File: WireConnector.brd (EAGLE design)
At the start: 15.2 x 20.3 mm, 2 parts

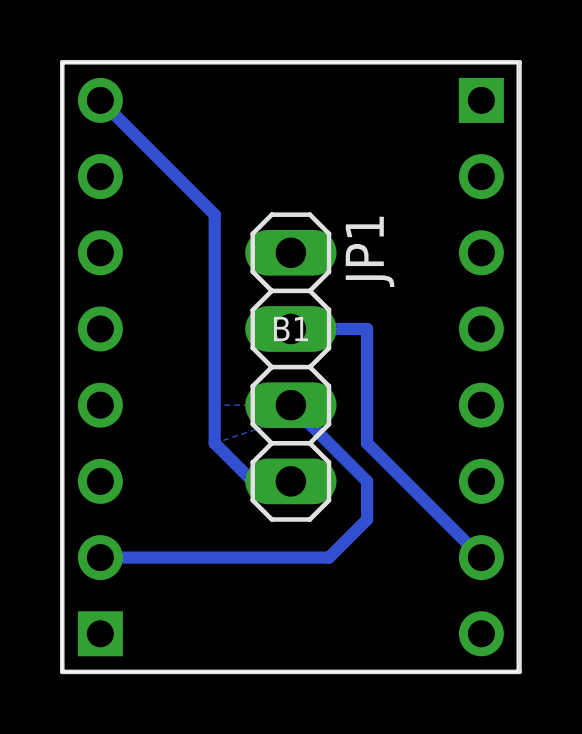
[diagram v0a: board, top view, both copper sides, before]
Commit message: Changed PWR connection position 2 Layer design GND Plate both sites Naming completed
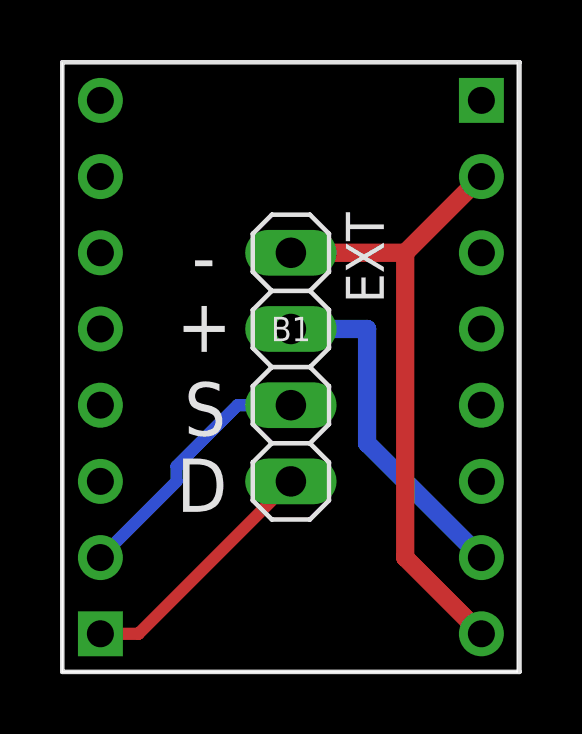
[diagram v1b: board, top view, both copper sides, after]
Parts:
- renumbered JP1 to EXT
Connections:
- net N$4: now also B1.DIR; no longer B1.EN
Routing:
- net GND: track 0.00 -> 21.2 mm
- net N$4: track 16.1 -> 8.45 mm
- net N$3: track 14.3 -> 8.75 mm
- added copper zone on layer 1, net GND
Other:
- board text added: "+"
- board text added: "-"
- board text added: "D"
- board text added: "S"
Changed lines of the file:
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@@
 <?xml version="1.0" encoding="utf-8"?>
 <!DOCTYPE eagle SYSTEM "eagle.dtd">
-<eagle version="7.2.0">
+<eagle version="7.7.0">
 <drawing>
 <settings>
@@
 <wire x1="26.67" y1="40.64" x2="41.834" y2="40.64" width="0" layer="20"/>
 <wire x1="41.834" y1="40.64" x2="41.834" y2="60.95" width="0" layer="20"/>
-<wire x1="41.834" y1="60.95" x2="26.67" y2="60.95" width="0" layer="20"/>
 <wire x1="26.67" y1="60.95" x2="26.67" y2="40.64" width="0" layer="20"/>
+<text x="30.988" y="53.594" size="1.778" layer="25">-</text>
+<text x="30.48" y="51.308" size="1.778" layer="25">+</text>
+<text x="30.734" y="48.514" size="1.778" layer="25">S</text>
+<text x="30.48" y="45.974" size="1.778" layer="25">D</text>
 </plain>
 <attributes>
@@
 </class>
 </classes>
-<designrules name="default">
+<designrules name="default *">
 <description language="de">&lt;b&gt;EAGLE Design Rules&lt;/b&gt;
 &lt;p&gt;
@@
 <param name="mdViaViaSameLayer" value="8mil"/>
 <param name="mnLayersViaInSmd" value="2"/>
-<param name="mdCopperDimension" value="40mil"/>
+<param name="mdCopperDimension" value="10mil"/>
 <param name="mdDrill" value="8mil"/>
 <param name="mdSmdStop" value="0mil"/>
@@
 <autorouter>
 <pass name="Default">
-<param name="RoutingGrid" value="50mil"/>
+<param name="RoutingGrid" value="12.5mil"/>
 <param name="AutoGrid" value="1"/>
 <param name="Efforts" value="0"/>
 <param name="TopRouterVariant" value="1"/>
 <param name="tpViaShape" value="round"/>
-<param name="PrefDir.1" value="a"/>
+<param name="PrefDir.1" value="-"/>
 <param name="PrefDir.2" value="0"/>
 <param name="PrefDir.3" value="0"/>
@@
 <param name="PrefDir.14" value="0"/>
 <param name="PrefDir.15" value="0"/>
-<param name="PrefDir.16" value="a"/>
+<param name="PrefDir.16" value="|"/>
 <param name="cfVia" value="8"/>
 <param name="cfNonPref" value="5"/>
@@
 <elements>
 <element name="B1" library="we-board" package="STEPSTICK_TP" value="STEPSTICK-TP" x="34.29" y="50.8"/>
-<element name="JP1" library="pinhead" package="1X04" value="" x="34.29" y="50.8" rot="R270"/>
+<element name="EXT" library="pinhead" package="1X04" value="" x="34.29" y="50.8" rot="R270"/>
 </elements>
 <signals>
@@
 </signal>
 <signal name="N$2" class="2">
-<contactref element="JP1" pad="2"/>
+<contactref element="EXT" pad="2"/>
 <contactref element="B1" pad="VIO"/>
-<wire x1="34.29" y1="52.07" x2="36.83" y2="52.07" width="0.4064" layer="16"/>
-<wire x1="36.83" y1="52.07" x2="36.83" y2="48.26" width="0.4064" layer="16"/>
-<wire x1="36.83" y1="48.26" x2="40.64" y2="44.45" width="0.4064" layer="16"/>
+<wire x1="34.29" y1="52.07" x2="36.83" y2="52.07" width="0.6096" layer="16"/>
+<wire x1="36.83" y1="52.07" x2="36.83" y2="48.26" width="0.6096" layer="16"/>
+<wire x1="36.83" y1="48.26" x2="40.64" y2="44.45" width="0.6096" layer="16"/>
 </signal>
 <signal name="N$3" class="1">
-<contactref element="JP1" pad="3"/>
+<contactref element="EXT" pad="3"/>
 <contactref element="B1" pad="STEP"/>
-<wire x1="34.29" y1="49.53" x2="36.83" y2="46.99" width="0.4064" layer="16"/>
-<wire x1="36.83" y1="46.99" x2="36.83" y2="45.72" width="0.4064" layer="16"/>
-<wire x1="36.83" y1="45.72" x2="35.56" y2="44.45" width="0.4064" layer="16"/>
-<wire x1="35.56" y1="44.45" x2="27.94" y2="44.45" width="0.4064" layer="16"/>
+<wire x1="27.94" y1="44.45" x2="30.48" y2="46.99" width="0.4064" layer="16"/>
+<wire x1="30.48" y1="46.99" x2="30.48" y2="47.498" width="0.4064" layer="16"/>
+<wire x1="30.48" y1="47.498" x2="32.512" y2="49.53" width="0.4064" layer="16"/>
+<wire x1="32.512" y1="49.53" x2="34.29" y2="49.53" width="0.4064" layer="16"/>
 </signal>
 <signal name="N$4" class="2">
-<contactref element="JP1" pad="4"/>
-<contactref element="B1" pad="EN"/>
-<wire x1="34.29" y1="46.99" x2="33.02" y2="46.99" width="0.4064" layer="16"/>
-<wire x1="33.02" y1="46.99" x2="31.75" y2="48.26" width="0.4064" layer="16"/>
-<wire x1="31.75" y1="48.26" x2="31.75" y2="55.88" width="0.4064" layer="16"/>
-<wire x1="31.75" y1="55.88" x2="27.94" y2="59.69" width="0.4064" layer="16"/>
+<contactref element="EXT" pad="4"/>
+<contactref element="B1" pad="DIR"/>
+<wire x1="34.29" y1="46.99" x2="29.21" y2="41.91" width="0.4064" layer="1"/>
+<wire x1="29.21" y1="41.91" x2="27.94" y2="41.91" width="0.4064" layer="1"/>
 </signal>
 <signal name="GND" class="2">
-<polygon width="0.4064" layer="16" spacing="1.4224" pour="cutout" isolate="1.4224" orphans="yes">
-<vertex x="31.75" y="48.26"/>
-<vertex x="31.75" y="49.53"/>
-<vertex x="35.56" y="49.53"/>
-</polygon>
 <contactref element="B1" pad="GND@2"/>
 <contactref element="B1" pad="GND@1"/>
-<contactref element="JP1" pad="1"/>
+<contactref element="EXT" pad="1"/>
 <polygon width="0.254" layer="16" spacing="1.4224" isolate="0.4064" orphans="yes">
 <vertex x="26.67" y="60.96"/>
@@
 <vertex x="26.67" y="40.64"/>
 </polygon>
-<wire x1="40.64" y1="41.91" x2="34.29" y2="54.61" width="0" layer="19" extent="1-1"/>
+<wire x1="34.29" y1="54.61" x2="38.1" y2="54.61" width="0.6096" layer="1"/>
+<wire x1="38.1" y1="54.61" x2="40.64" y2="57.15" width="0.6096" layer="1"/>
+<wire x1="38.1" y1="54.61" x2="38.1" y2="44.45" width="0.6096" layer="1"/>
+<wire x1="38.1" y1="44.45" x2="40.64" y2="41.91" width="0.6096" layer="1"/>
+<polygon width="0.3048" layer="1" isolate="0.4064">
+<vertex x="41.91" y="40.64"/>
+<vertex x="30.226" y="40.64"/>
+<vertex x="26.67" y="40.64"/>
+</polygon>
+<polygon width="0.254" layer="1" isolate="0.4064">
+<vertex x="26.67" y="60.96"/>
+<vertex x="41.91" y="60.96"/>
+<vertex x="41.91" y="45.974"/>
+<vertex x="41.91" y="40.64"/>
+<vertex x="27.94" y="40.64"/>
+<vertex x="26.67" y="40.64"/>
+</polygon>
 </signal>
 </signals>
